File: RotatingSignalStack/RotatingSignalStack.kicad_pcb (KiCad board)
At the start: 2 copper layers, 66.5 x 56.4 mm, 96 parts, among them IC2 STM32H562RIT6, J1 Conn_01x06, J2 Conn_01x04, J3 RJ45_LED_Shielded, J4 Conn_01x09, SW1 SW_Push, SW2 Boot Switch, SW5 SW_Push, SW6 SW_Push, SW7 SW_Push, T1 GMG116S1202R, U1 TMAG5273C1QDBVR, U2 AP63203WU-7, U3 SN65HVD232, U4 DP83825I, U5 SG-210STF 50.0000ML0, U6 USBLC6-2SC6, U7 USBLC6-4SC6, U8 OKI-78SR-3.3_1.5-W36-C

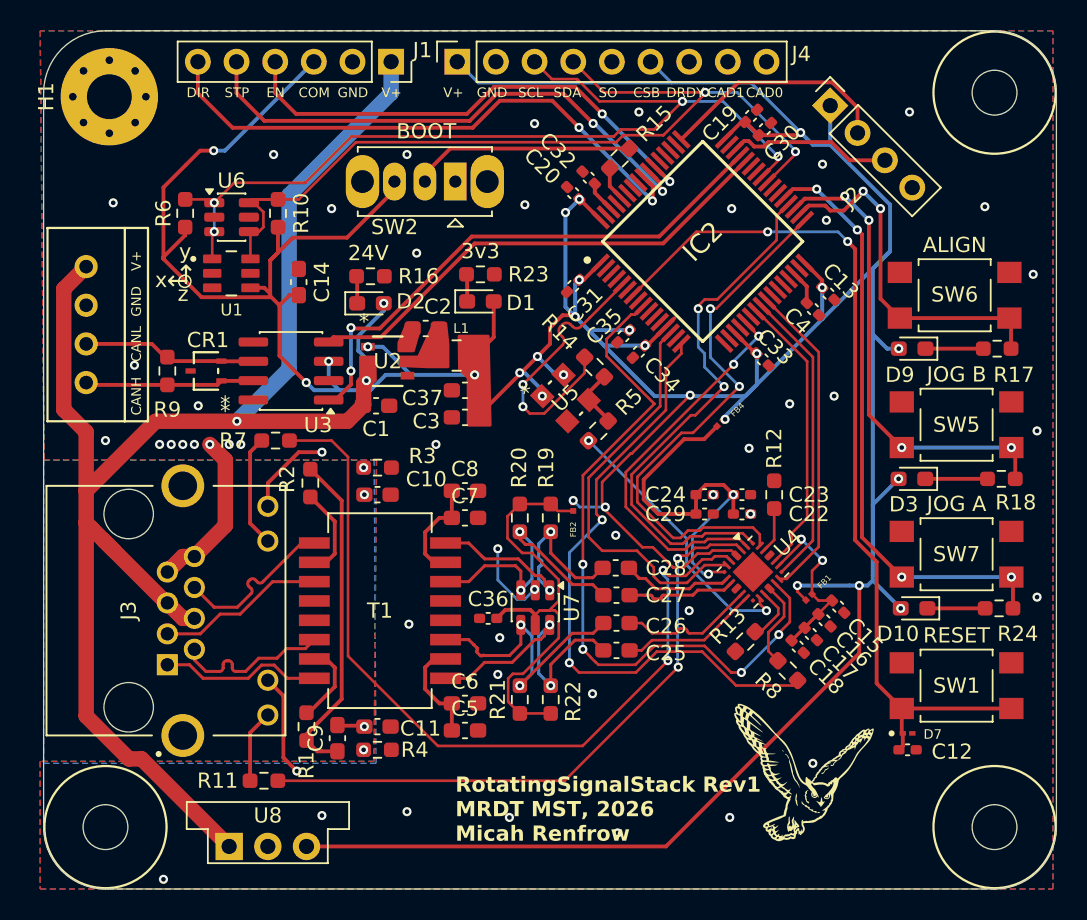
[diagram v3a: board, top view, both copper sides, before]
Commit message: mounting holes
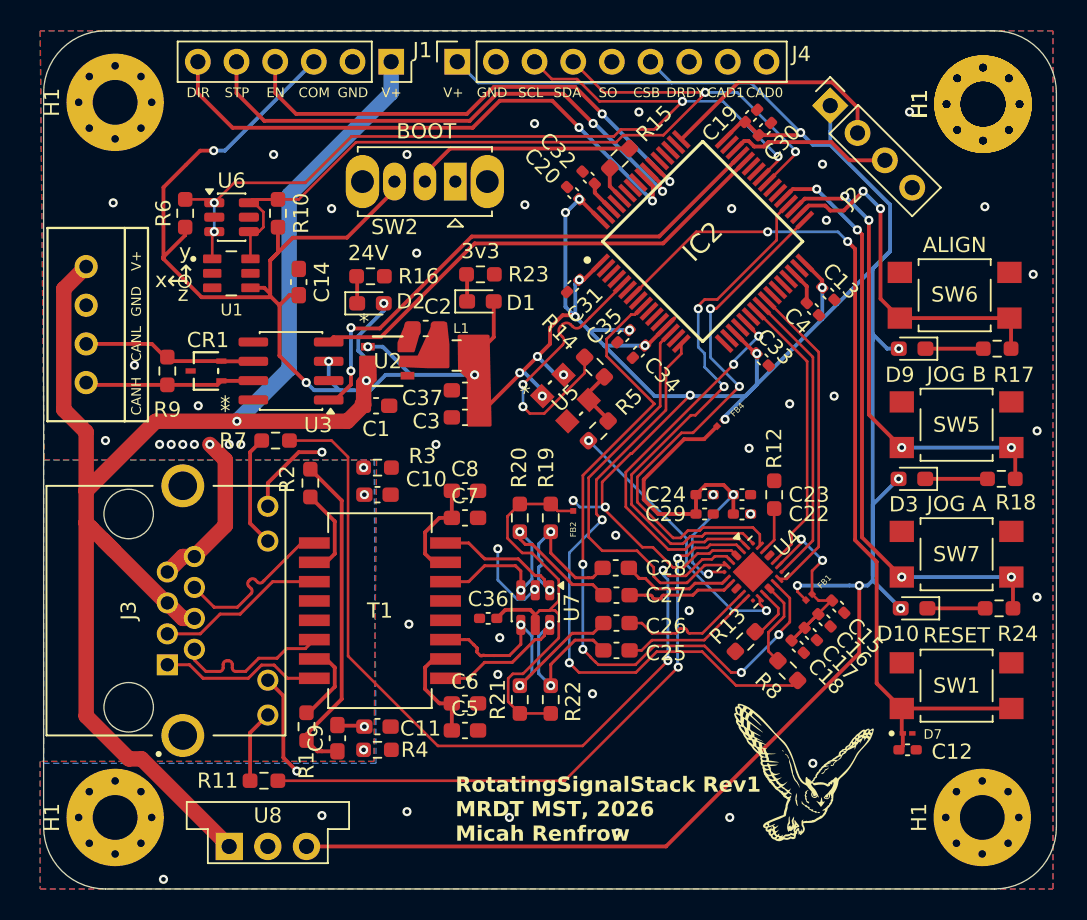
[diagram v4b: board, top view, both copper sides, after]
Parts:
- removed H2, H3, H4: MountingHole, MRDT_Drill_Holes:4_40_Hole_Corner
- added H1 (x2): MountingHole, MountingHole:MountingHole_3.2mm_M3_Pad_Via, F.Cu at (185.9, 58.7)
- added H1: MountingHole, MountingHole:MountingHole_3.2mm_M3_Pad_Via, F.Cu at (185.9, 105.5)
- added H1: MountingHole, MountingHole:MountingHole_3.2mm_M3_Pad_Via, F.Cu at (128.9, 105.5)
- added H1: MountingHole, MountingHole:MountingHole_3.2mm_M3_Pad_Via, F.Cu at (128.9, 58.5)
- moved H1 57.4 mm to (185.9, 58.7)

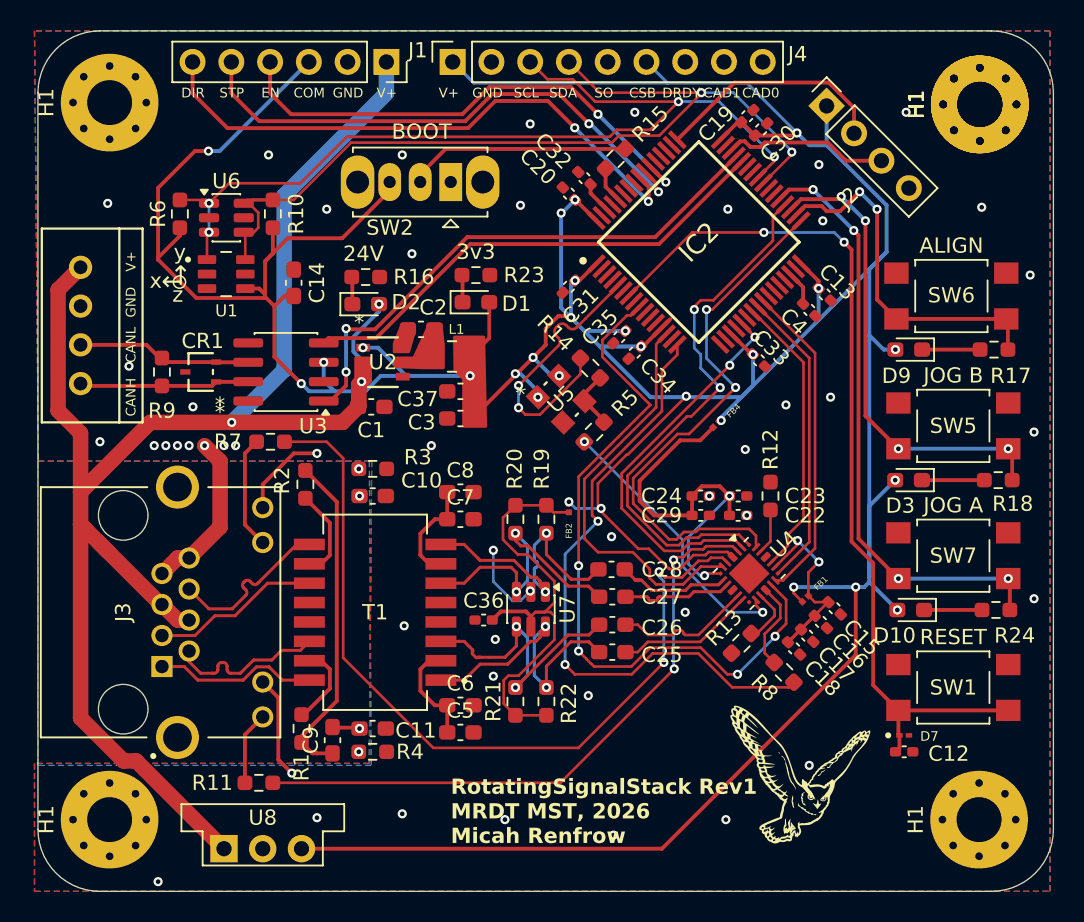
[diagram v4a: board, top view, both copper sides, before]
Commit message: mounting holes aligned and measurements
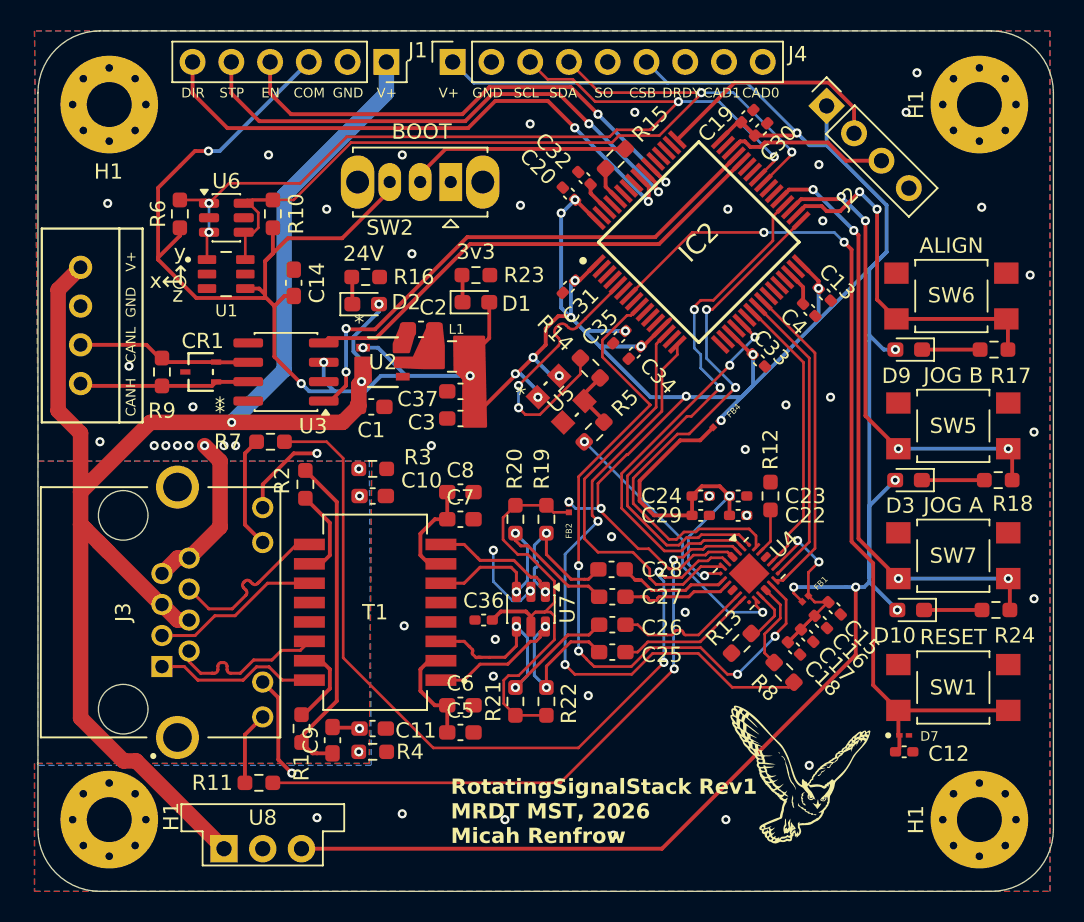
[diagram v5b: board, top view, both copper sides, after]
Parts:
- removed the H1 at (185.9, 58.7) (x3)
- added H1: MountingHole, MountingHole:MountingHole_3.2mm_M3_Pad_Via, F.Cu at (185.9, 58.7)
- moved H1 0.13 mm to (128.9, 58.7)

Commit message: final layout
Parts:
- removed D7: ESDALC6V1-1U2, SignalStack:DIODE_ESDALC6V1-1U2
- removed the H1 at (185.9, 105.5)
- removed the H1 at (128.9, 105.5)
- removed the H1 at (128.9, 58.7)
- removed SW2: Boot Switch, Button_Switch_THT:SW_Slide_SPDT_Straight_CK_OS102011MS2Q
- added H2: MountingHole, MountingHole:MountingHole_3.2mm_M3_Pad_Via, F.Cu at (128.9, 105.5)
- added H3: MountingHole, MountingHole:MountingHole_3.2mm_M3_Pad_Via, F.Cu at (128.9, 58.7)
- added H4: MountingHole, MountingHole:MountingHole_3.2mm_M3_Pad_Via, F.Cu at (185.9, 105.5)
- added JP1: Jumper_3_Bridged12, Connector_PinHeader_2.54mm:PinHeader_1x03_P2.54mm_Vertical, F.Cu at (149.4, 65.3)
- C12: footprint Capacitor_SMD:C_0402_1005Metric_Pad0.74x0.62mm_HandSolder -> Capacitor_SMD:C_0603_1608Metric_Pad1.08x0.95mm_HandSolder
- FB1, FB2, FB4: footprint SignalStack:BEADC0603X33N -> SignalStack:FB_MI0603L221R-10
- moved J4 49.5 mm to (146.8, 105.2)
- moved Conn1 8.36 mm to (130.4, 77.0), turned to 90 degrees
- moved J1 4.70 mm to (143.0, 58.3), turned to 90 degrees
- moved U8 2.29 mm to (136.4, 105.2)
- moved C3 1.26 mm to (152.8, 80.1)
- moved C37 1.26 mm to (152.8, 78.4)
- moved L1 1.26 mm to (152.2, 76.1)
- moved U2 1.26 mm to (147.7, 76.4)
- moved C1 1.26 mm to (146.9, 79.4)
- moved C2 0.97 mm to (150.2, 73.8)
- moved D10 0.91 mm to (180.5, 91.8)
- moved D9 0.91 mm to (180.4, 74.7)
- moved R24 0.91 mm to (186.1, 91.8)
- moved SW6 0.91 mm to (183.2, 71.2)
- moved D3 0.91 mm to (180.3, 83.3)
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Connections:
- H1 pad 1: (no net) -> GND
- IC2 pad 54: EN -> DIR
- IC2 pad 56: DIR -> EN
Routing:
- net +3V3: track 307.7 -> 265.9 mm
- net SCL: track 59.6 -> 98.8 mm, vias 4 -> 5
- net SDA: track 59.7 -> 98.8 mm, vias 2 -> 3
- net DIR: track 38.2 -> 13.3 mm
- net STP: track 35.9 -> 15.9 mm
- net EN: track 33.3 -> 18.2 mm
- net VBUS: track 111.7 -> 101.0 mm, vias 3 -> 2
- net /CAN/CANH: track 11.2 -> 14.3 mm, vias 0 -> 1
- net Net-(JP1-C): track 14.6 -> 11.9 mm
- net /CAN/CANL: track 11.5 -> 10.1 mm
- net Net-(IC2-NRST): track 58.3 -> 57.3 mm
- net Net-(U4-VDDA3V3): track 25.0 -> 24.2 mm
- net Net-(U4-VDDIO): track 15.7 -> 15.0 mm
- net /Buttons/JOG B: track 31.1 -> 31.7 mm, vias 4 -> 2
- net /Buttons/JOG A: vias 4 -> 2
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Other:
- board size 66.5 x 56.4 mm -> 64.1 x 54 mm

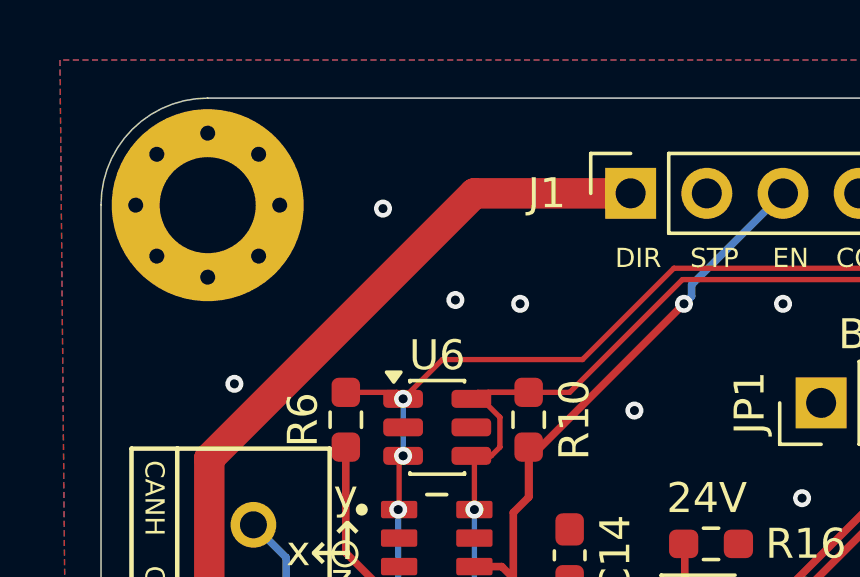
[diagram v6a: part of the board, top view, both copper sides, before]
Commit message: silkscreens and signature
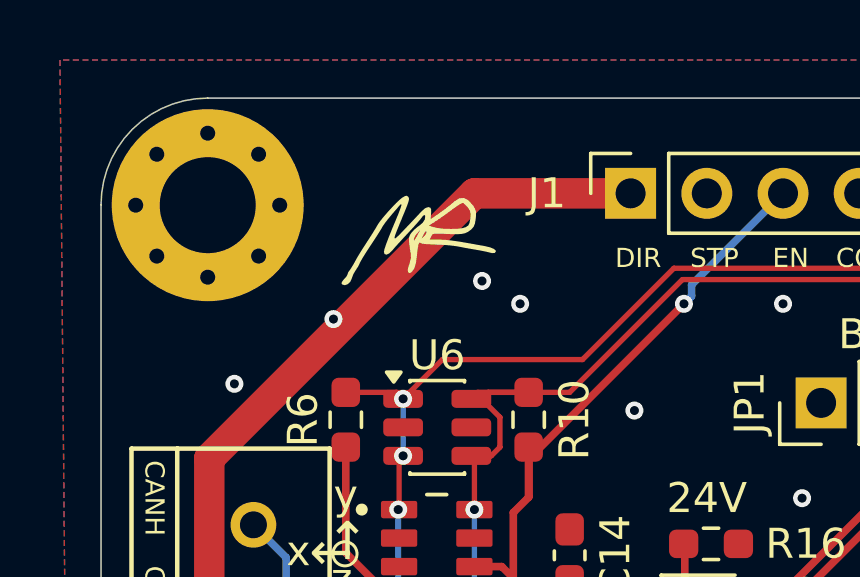
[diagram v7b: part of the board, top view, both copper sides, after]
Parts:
- added G***: LOGO, LOGO, F.Cu at (147.1, 49.1)
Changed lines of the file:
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@@
 		)
 	)
+	(footprint "LOGO"
+		(layer "F.Cu")
+		(at 147.066 49.149)
+		(property "Reference" "G***"
+			(at 0 0 0)
+			(layer "F.SilkS")
+			(hide yes)
+			(effects
+				(font
+					(size 1.5 1.5)
+					(thickness 0.3)
+				)
+			)
+		)
+		(property "Value" "LOGO"
+			(at 0.75 0 0)
+			(layer "F.SilkS")
+			(hide yes)
+			(effects
+				(font
+					(size 1.5 1.5)
+					(thickness 0.3)
+				)
+			)
+		)
+		(property "Datasheet" ""
+			(at 0 0 0)
+			(layer "F.Fab")
+			(hide yes)
+			(effects
+				(font
+					(size 1.27 1.27)
+					(thickness 0.15)
+				)
+			)
+		)
+		(property "Description" ""
+			(at 0 0 0)
+			(layer "F.Fab")
+			(hide yes)
+			(effects
+				(font
+					(size 1.27 1.27)
+					(thickness 0.15)
+				)
+			)
+		)
+		(attr board_only exclude_from_pos_files exclude_from_bom)
+		(fp_poly
+			(pts
+				(xy -11.479442 9.25616) (xy -11.47698 9.258601) (xy -11.455241 9.292705) (xy -11.451905 9.344543)
+				(xy -11.47065 9.427552) (xy -11.515152 9.555168) (xy -11.589088 9.740826) (xy -11.647581 9.882015)
+				(xy -11.770326 10.176488) (xy -11.859484 10.395533) (xy -11.914421 10.544068) (xy -11.934503 10.627008)
+				(xy -11.919094 10.649269) (xy -11.867561 10.615767) (xy -11.779267 10.531418) (xy -11.653579 10.401138)
+				(xy -11.589265 10.333675) (xy -11.425427 10.161391) (xy -11.268485 9.995443) (xy -11.136032 9.854489)
+				(xy -11.045662 9.757191) (xy -11.044302 9.755706) (xy -10.917855 9.641075) (xy -10.816057 9.602645)
+				(xy -10.797758 9.60374) (xy -10.738843 9.623018) (xy -10.714137 9.674779) (xy -10.713593 9.783798)
+				(xy -10.715047 9.807743) (xy -10.727359 9.998221) (xy -10.6065 9.919735) (xy -10.441684 9.80685)
+				(xy -10.258822 9.672611) (xy -10.086072 9.538407) (xy -9.951592 9.425629) (xy -9.929815 9.405701)
+				(xy -9.778015 9.309576) (xy -9.624369 9.297995) (xy -9.478686 9.370852) (xy -9.436244 9.411025)
+				(xy -9.312604 9.551922) (xy -9.242756 9.665164) (xy -9.215679 9.780891) (xy -9.220352 9.929242)
+				(xy -9.226351 9.985076) (xy -9.252286 10.146257) (xy -9.292839 10.251989) (xy -9.361554 10.333652)
+				(xy -9.386037 10.355095) (xy -9.478902 10.424415) (xy -9.575045 10.470601) (xy -9.693029 10.496897)
+				(xy -9.851416 10.506549) (xy -10.06877 10.502801) (xy -10.199029 10.497218) (xy -10.40435 10.488258)
+				(xy -10.539909 10.486472) (xy -10.622666 10.494538) (xy -10.66958 10.515138) (xy -10.697609 10.550949)
+				(xy -10.711138 10.578136) (xy -10.759694 10.681025) (xy -10.464162 10.681025) (xy -10.29768 10.689103)
+				(xy -10.077761 10.710954) (xy -9.836054 10.743001) (xy -9.654144 10.772529) (xy -9.429935 10.812365)
+				(xy -9.215928 10.850315) (xy -9.038543 10.881698) (xy -8.936307 10.899713) (xy -8.754041 10.942754)
+				(xy -8.622718 10.996189) (xy -8.557758 11.053128) (xy -8.553505 11.07076) (xy -8.587673 11.129321)
+				(xy -8.68488 11.135949) (xy -8.754757 11.119157) (xy -8.859235 11.093041) (xy -9.016626 11.060629)
+				(xy -9.193989 11.028675) (xy -9.204787 11.02688) (xy -9.418101 10.990142) (xy -9.647409 10.948407)
+				(xy -9.817664 10.915695) (xy -9.989713 10.88998) (xy -10.212497 10.868654) (xy -10.44992 10.854805)
+				(xy -10.56713 10.851584) (xy -10.75885 10.845341) (xy -10.916568 10.833737) (xy -11.021202 10.818577)
+				(xy -11.053578 10.805632) (xy -11.094666 10.776937) (xy -11.129931 10.83368) (xy -11.15952 10.976286)
+				(xy -11.1813 11.176978) (xy -11.21359 11.427169) (xy -11.262032 11.610611) (xy -11.293093 11.676132)
+				(xy -11.376005 11.778965) (xy -11.442947 11.805887) (xy -11.484573 11.767574) (xy -11.491537 11.6747)
+				(xy -11.454493 11.53794) (xy -11.441267 11.506896) (xy -11.386169 11.300025) (xy -11.392306 11.172735)
+				(xy -11.428383 10.941789) (xy -11.448838 10.778665) (xy -11.453142 10.668974) (xy -11.28889 10.668974)
+				(xy -11.287028 10.71238) (xy -11.274818 10.715342) (xy -11.242325 10.666608) (xy -11.23823 10.659316)
+				(xy -11.037549 10.659316) (xy -10.941 10.566146) (xy -10.878675 10.483147) (xy -10.864257 10.414267)
+				(xy -10.864286 10.414181) (xy -10.893187 10.407416) (xy -10.942803 10.473654) (xy -10.960836 10.50735)
+				(xy -11.037549 10.659316) (xy -11.23823 10.659316) (xy -11.179613 10.554927) (xy -11.165335 10.52906)
+				(xy -11.069511 10.355384) (xy -11.1792 10.477207) (xy -11.251614 10.575149) (xy -11.28791 10.658552)
+				(xy -11.28889 10.668974) (xy -11.453142 10.668974) (xy -11.453271 10.665694) (xy -11.441283 10.585207)
+				(xy -11.412473 10.519531) (xy -11.37628 10.464707) (xy -11.274294 10.35185) (xy -11.144454 10.244622)
+				(xy -11.115979 10.225611) (xy -11.110832 10.221318) (xy -10.789573 10.221318) (xy -10.615898 10.274159)
+				(xy -10.45925 10.306034) (xy -10.259759 10.324695) (xy -10.043405 10.330229) (xy -9.836168 10.322721)
+				(xy -9.664028 10.302255) (xy -9.556283 10.27069) (xy -9.479947 10.217539) (xy -9.436533 10.139858)
+				(xy -9.41102 10.008583) (xy -9.407947 9.983639) (xy -9.397589 9.839074) (xy -9.415397 9.739044)
+				(xy -9.470657 9.643326) (xy -9.493636 9.612436) (xy -9.575864 9.521079) (xy -9.646598 9.469529)
+				(xy -9.663538 9.465299) (xy -9.722685 9.49019) (xy -9.830123 9.556509) (xy -9.966108 9.651722) (xy -10.01659 9.6894)
+				(xy -10.192228 9.819131) (xy -10.37883 9.951424) (xy -10.538519 10.059472) (xy -10.55077 10.067409)
+				(xy -10.789573 10.221318) (xy -11.110832 10.221318) (xy -10.996296 10.12579) (xy -10.927027 10.018714)
+				(xy -10.923147 10.005794) (xy -10.910344 9.898471) (xy -10.93639 9.862033) (xy -10.99197 9.902446)
+				(xy -11.021321 9.942906) (xy -11.077274 10.015169) (xy -11.179373 10.134218) (xy -11.31364 10.284179)
+				(xy -11.466098 10.449181) (xy -11.483327 10.467513) (xy -11.644728 10.640589) (xy -11.797404 10.807234)
+				(xy -11.924495 10.948862) (xy -12.009139 11.046888) (xy -12.01118 11.049367) (xy -12.115875 11.150107)
+				(xy -12.206135 11.189734) (xy -12.267902 11.166109) (xy -12.287522 11.091417) (xy -12.268871 11.001751)
+				(xy -12.213441 10.835874) (xy -12.122018 10.595866) (xy -11.995386 10.283809) (xy -11.871919 9.989945)
+				(xy -11.797285 9.808344) (xy -11.740138 9.65753) (xy -11.70652 9.554297) (xy -11.701366 9.515956)
+				(xy -11.735634 9.512336) (xy -11.767794 9.550996) (xy -11.843587 9.639617) (xy -11.949663 9.762631)
+				(xy -12.011783 9.834359) (xy -12.137902 9.985519) (xy -12.248248 10.128073) (xy -12.325088 10.238728)
+				(xy -12.342319 10.268547) (xy -12.391334 10.353133) (xy -12.477596 10.491499) (xy -12.589603 10.665561)
+				(xy -12.715852 10.857237) (xy -12.736549 10.888248) (xy -12.860224 11.076863) (xy -12.967297 11.247011)
+				(xy -13.04762 11.382071) (xy -13.091046 11.465422) (xy -13.094403 11.474402) (xy -13.141297 11.573876)
+				(xy -13.215894 11.690201) (xy -13.226913 11.704993) (xy -13.303975 11.833928) (xy -13.354419 11.967658)
+				(xy -13.356658 11.977903) (xy -13.406727 12.090361) (xy -13.491546 12.170537) (xy -13.587788 12.206397)
+				(xy -13.672124 12.185906) (xy -13.700009 12.155039) (xy -13.690309 12.098504) (xy -13.629857 12.018821)
+				(xy -13.615734 12.005146) (xy -13.540049 11.921146) (xy -13.503788 11.853657) (xy -13.503249 11.84797)
+				(xy -13.47663 11.774258) (xy -13.442438 11.726495) (xy -13.388111 11.650668) (xy -13.313958 11.529624)
+				(xy -13.26405 11.440854) (xy -13.204898 11.333174) (xy -13.146967 11.232343) (xy -13.080104 11.121892)
+				(xy -12.994154 10.985352) (xy -12.878964 10.806252) (xy -12.755449 10.615897) (xy -12.65572 10.459641)
+				(xy -12.568867 10.318467) (xy -12.51062 10.21807) (xy -12.502909 10.203419) (xy -12.437416 10.103307)
+				(xy -12.326193 9.961723) (xy -12.186078 9.797409) (xy -12.033908 9.629109) (xy -11.886522 9.475565)
+				(xy -11.760756 9.355523) (xy -11.689346 9.297782) (xy -11.589692 9.236035) (xy -11.529138 9.223898)
+			)
+			(stroke
+				(width 0)
+				(type solid)
+			)
+			(fill yes)
+			(layer "F.SilkS")
+		)
+		(embedded_fonts no)
+	)
 	(footprint "Capacitor_SMD:C_0402_1005Metric_Pad0.74x0.62mm_HandSolder"
 		(layer "F.Cu")
@@
 	)
 	(via
-		(at 137.16 61.849)
-		(size 0.6)
-		(drill 0.3)
-		(layers "F.Cu" "B.Cu")
-		(free yes)
-		(net 1)
-	)
-	(via
 		(at 154.051 87.884)
 		(size 0.6)
@@
 	)
 	(via
+		(at 138.049 61.214)
+		(size 0.6)
+		(drill 0.3)
+		(layers "F.Cu" "B.Cu")
+		(free yes)
+		(net 1)
+	)
+	(via
 		(at 156.6418 71.0946)
 		(size 0.6)
@@
 	)
 	(via
+		(at 133.096 62.484)
+		(size 0.6)
+		(drill 0.3)
+		(layers "F.Cu" "B.Cu")
+		(free yes)
+		(net 1)
+	)
+	(via
 		(at 174.752 101.981)
 		(size 0.6)
@@
 		(size 0.6)
 		(drill 0.3)
-		(layers "F.Cu" "B.Cu")
-		(free yes)
-		(net 1)
-	)
-	(via
-		(at 134.747 58.801)
-		(size 0.6)
-		(drill 0.3)
